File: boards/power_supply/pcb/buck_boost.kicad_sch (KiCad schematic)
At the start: 30 parts

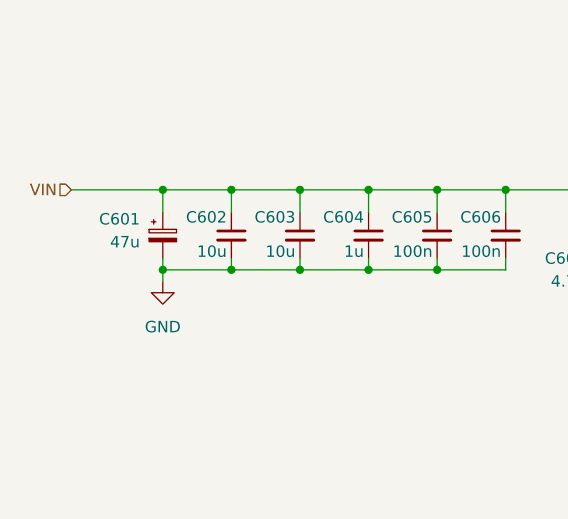
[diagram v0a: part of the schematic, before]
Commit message: psu schematic capture
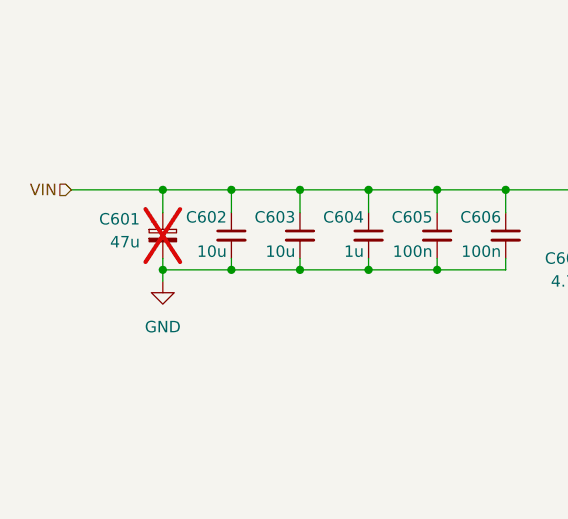
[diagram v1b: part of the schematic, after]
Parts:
- C601: now not fitted
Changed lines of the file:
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@@
 		(in_bom yes)
 		(on_board yes)
-		(dnp no)
+		(dnp yes)
 		(property "Reference" "C601"
 			(at 52.07 79.4638 0)

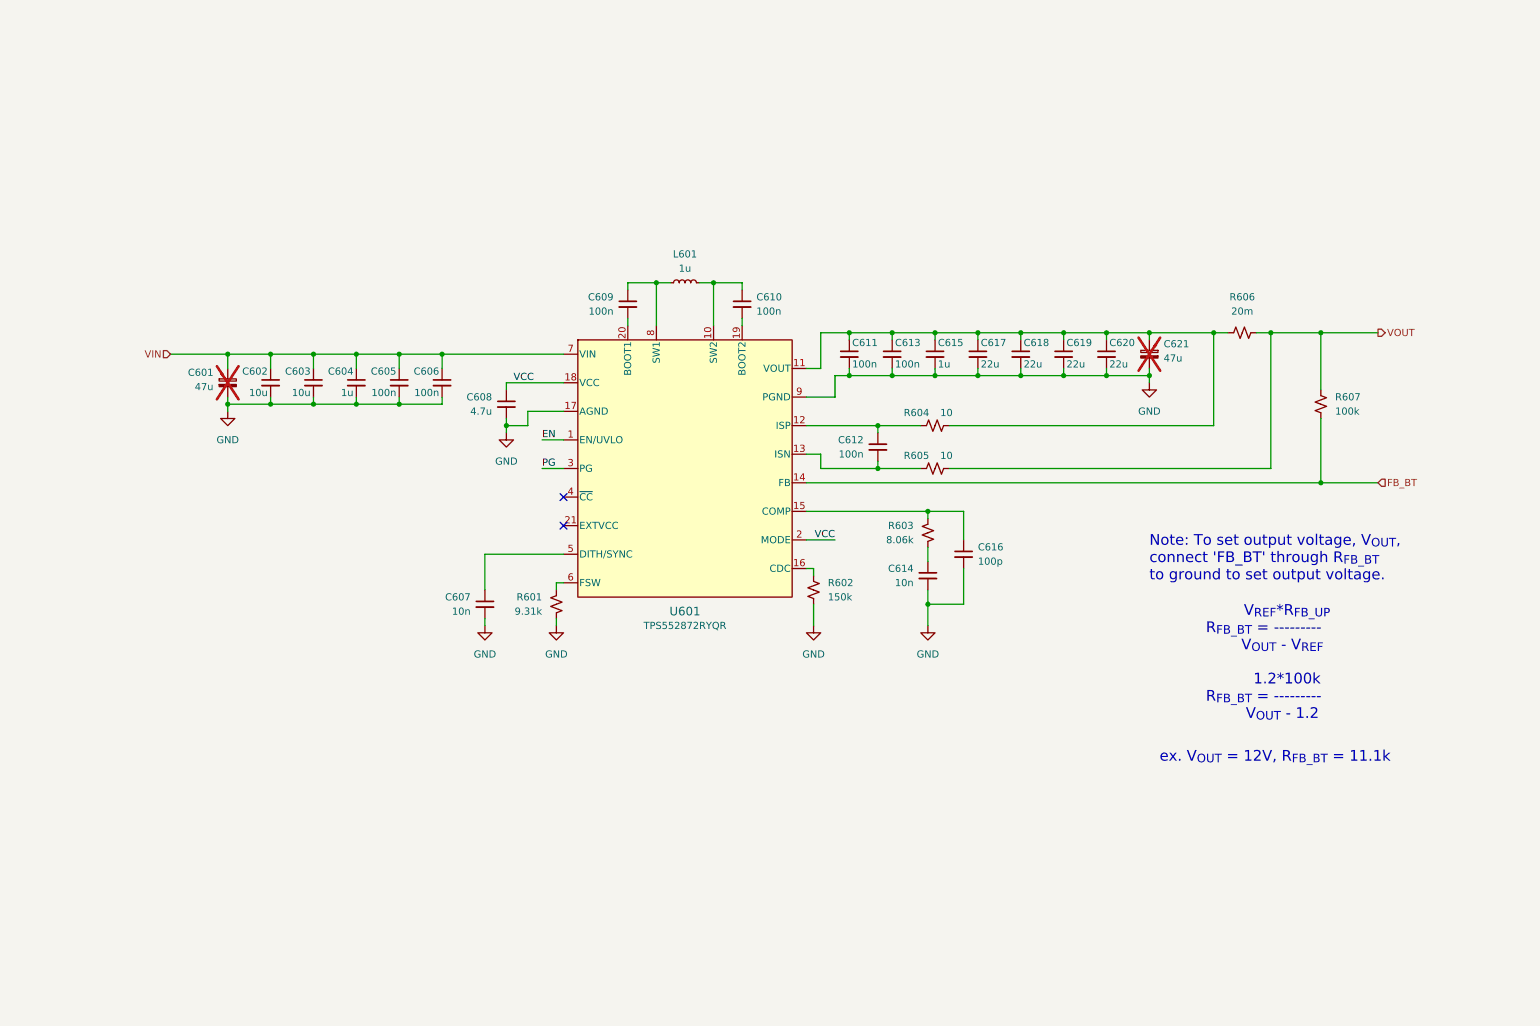
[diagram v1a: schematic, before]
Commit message: psu schematic capture
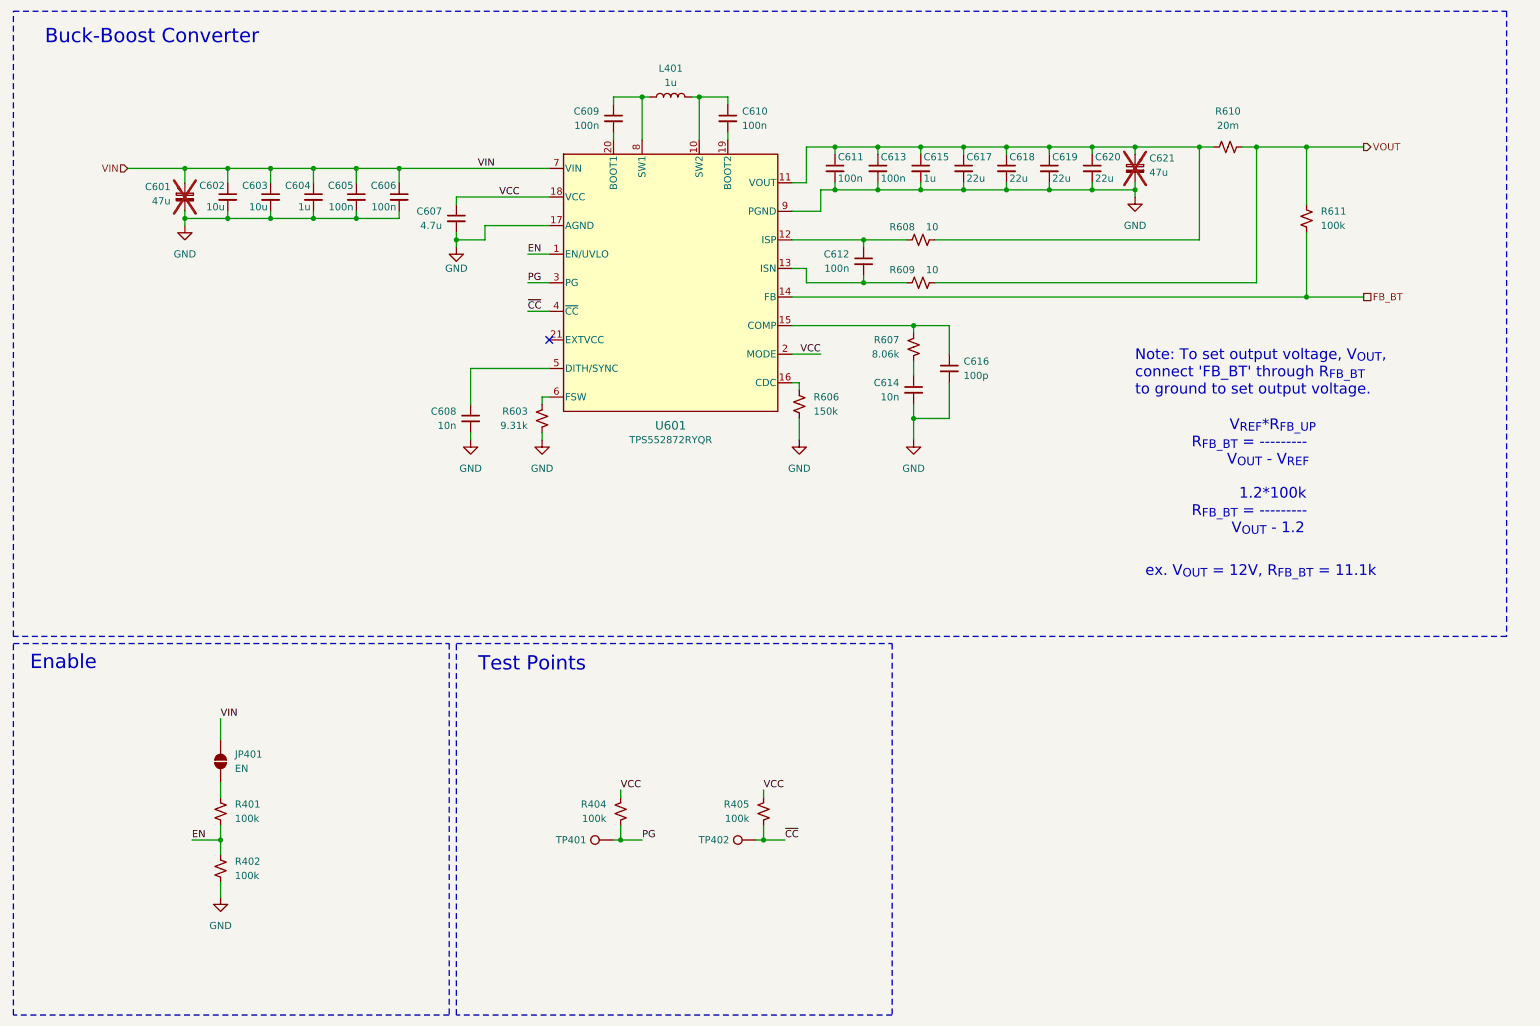
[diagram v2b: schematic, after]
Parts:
- removed L601: 1u, symbol Device:L_Small
- added JP401: EN, symbol Jumper:SolderJumper_2_Open
- added L401: 1u, symbol Device:L
- added R401, R402, R404, R405: 100k, symbol Device:R_Small_US
- added TP401, TP402: TestPoint, symbol Connector:TestPoint
- renumbered C608 to C607, C607 to C608, R601 to R603, R602 to R606, R603 to R607, R604 to R608, R605 to R609, R606 to R610, R607 to R611
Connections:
- net EN: now also R401.2, R402.1
- net GND: now also R402.2
- net PG: now also R404.2, TP401.1
- net VCC: now also R404.1, R405.1
- net VIN: now also JP401.2 (B)
- net at C610.1, U601.10 (SW2): now also L401.2
- net at C609.1, U601.8 (SW1): now also L401.1
- net ~{CC}: now reaches U601.4 (~{CC})
- net ~{CC}: now also R405.2, TP402.1
- new net: JP401.1 (A), R401.1
- no-connect marks 2 -> 1
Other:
- note added: "Buck-Boost Converter"
- note added: "Enable"
- note added: "Test Points"
- moved on the sheet: C601, C602, C603, C604, C605, C606, C607, C608, C609, C610, C611, C612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

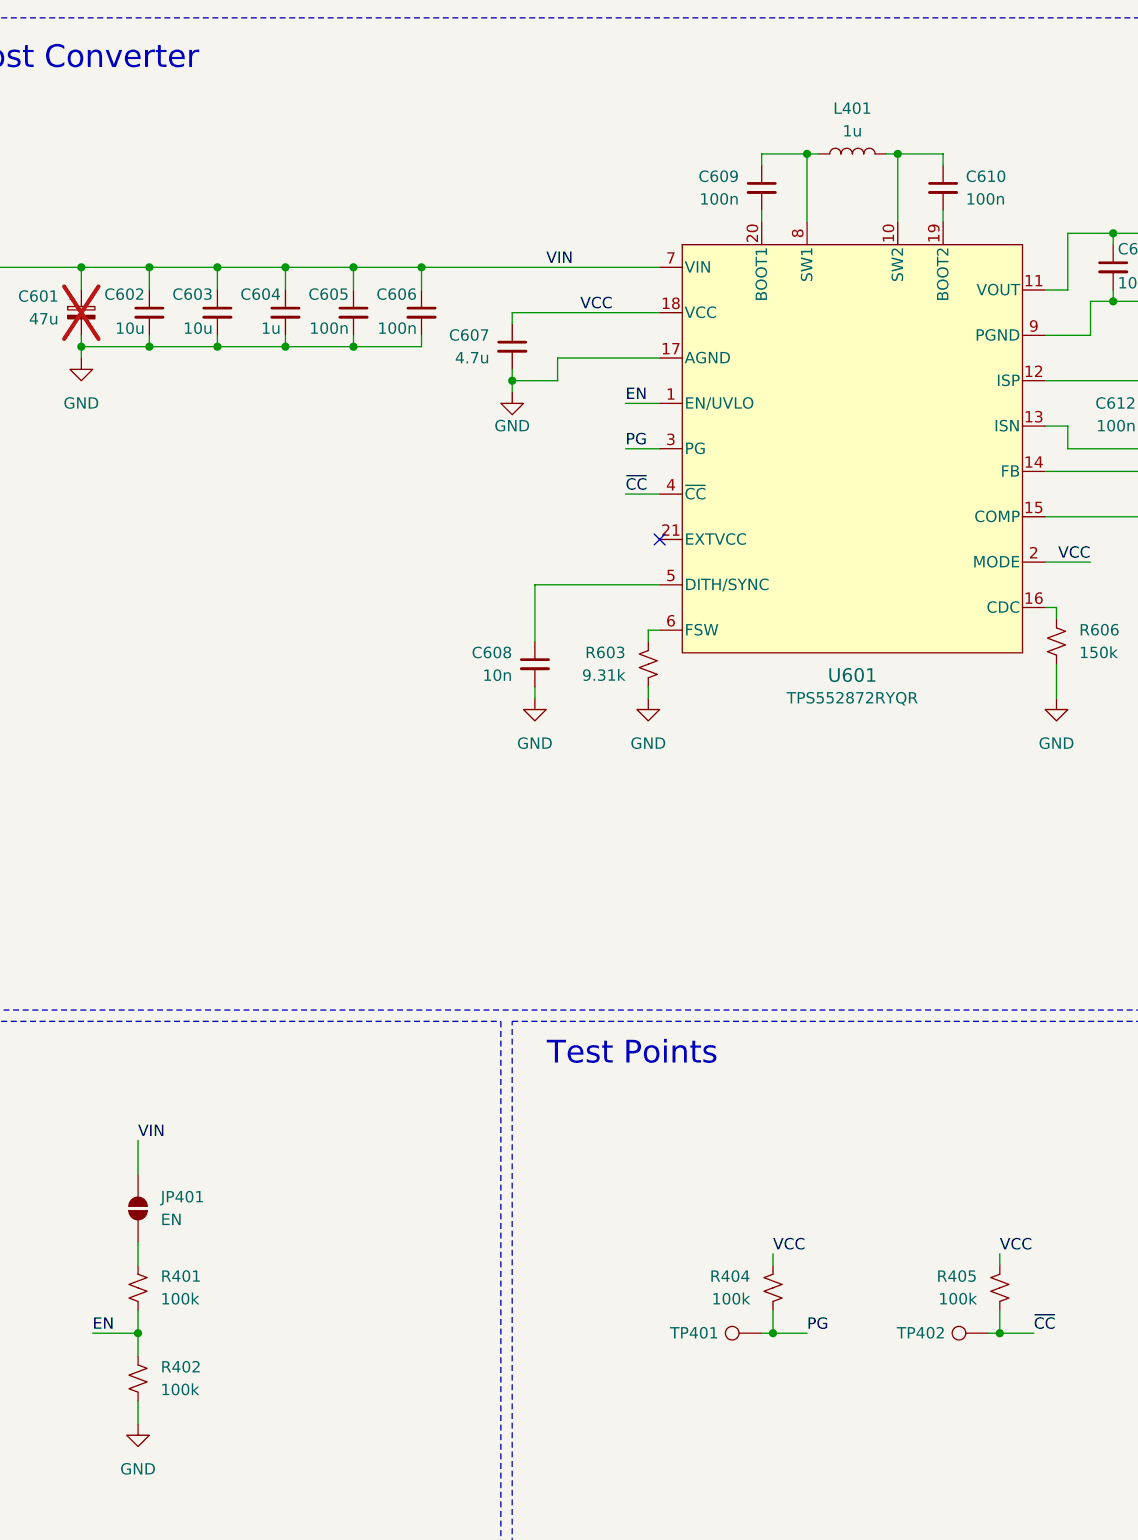
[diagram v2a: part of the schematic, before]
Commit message: psu component selection
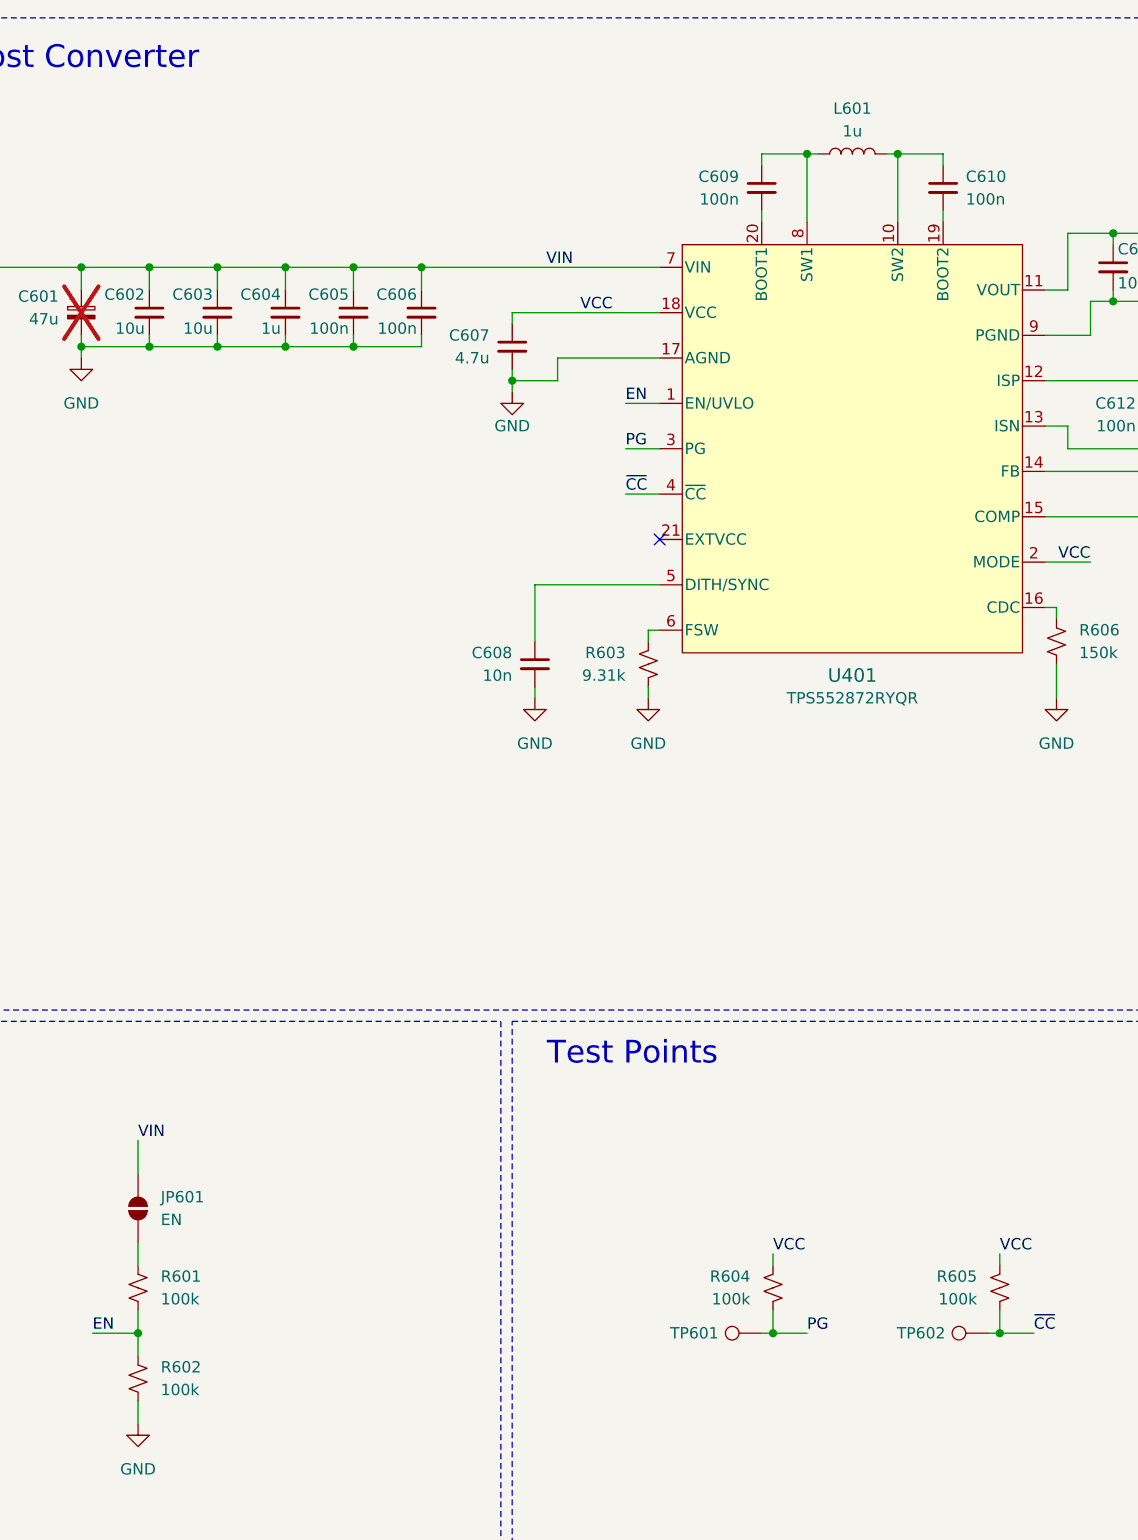
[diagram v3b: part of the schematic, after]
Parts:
- removed U601: ~, VQFN21_RYQ_TEX, symbol TPS552872RYQR:TPS552872RYQR
- added U401: ~, VQFN21_RYQ_TEX, symbol TPS552872RYQR:TPS552872RYQR
- renumbered JP401 to JP601, L401 to L601, R401 to R601, R402 to R602, R404 to R604, R405 to R605, TP401 to TP601, TP402 to TP602
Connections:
- net EN: now also U401.1 (EN/UVLO)
- net FB_BT: now also U401.14 (FB)
- net GND: now also U401.17 (AGND), U401.9 (PGND)
- net PG: now also U401.3 (PG)
- net VCC: now also U401.18 (VCC), U401.2 (MODE)
- net VIN: now also U401.7 (VIN)
- net ~{CC}: now also U401.4 (~{CC})
- net at R606.1: now also U401.16 (CDC)
- net at C611.1, C613.1, C615.1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: now also U401.11 (VOUT)
- net at C612.2, R609.2: now also U401.13 (ISN)
- net at C616.1, R607.1: now also U401.15 (COMP)
- net at C610.1, L601.2: now also U401.10 (SW2)
- net at C610.2: now also U401.19 (BOOT2)
- net at C608.1: now also U401.5 (DITH/SYNC)
- net at C609.1, L601.1: now also U401.8 (SW1)
- net at C609.2: now also U401.20 (BOOT1)
- net at C612.1, R608.2: now also U401.12 (ISP)
- net at R603.1: now also U401.6 (FSW)
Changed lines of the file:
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@@
 		(dnp no)
 		(fields_autoplaced yes)
-		(property "Reference" "#PWR0402"
+		(property "Reference" "#PWR0602"
 			(at 53.34 179.07 0)
 			(effects
@@
 	)
 	(symbol
+		(lib_id "TPS552872RYQR:TPS552872RYQR")
+		(at 111.76 43.18 0)
+		(unit 1)
+		(exclude_from_sim no)
+		(in_bom yes)
+		(on_board yes)
+		(dnp no)
+		(fields_autoplaced yes)
+		(property "Reference" "U401"
+			(at 133.35 88.9 0)
+			(effects
+				(font
+					(size 1.524 1.524)
+				)
+			)
+		)
+		(property "Value" "~"
+			(at 132.842 90.424 0)
+			(effects
+				(font
+					(size 1.524 1.524)
+				)
+				(hide yes)
+			)
+		)
+		(property "Footprint" "VQFN21_RYQ_TEX"
+			(at 133.35 93.98 0)
+			(effects
+				(font
+					(size 1.524 1.524)
+				)
+				(hide yes)
+			)
+		)
+		(property "Datasheet" "https://www.ti.com/lit/ds/symlink/tps552872.pdf?ts=1701344503514&ref_url=https%253A%252F%252Fwww.ti.com%252Fproduct%252FTPS552872"
+			(at 131.826 27.432 0)
+			(effects
+				(font
+					(size 1.524 1.524)
+				)
+				(hide yes)
+			)
+		)
+		(property "Description" "Buck-Boost Switching Regulator IC Positive Adjustable 0.8V 1 Output 2.5A 21-PowerVFQFN"
+			(at 130.81 24.384 0)
+			(effects
+				(font
+					(size 1.27 1.27)
+				)
+				(hide yes)
+			)
+		)
+		(property "MPN" "TPS552872RYQR"
+			(at 133.35 91.44 0)
+			(effects
+				(font
+					(size 1.27 1.27)
+				)
+			)
+		)
+		(pin "20"
+		)
+		(pin "21"
+		)
+		(pin "15"
+		)
+		(pin "7"
+		)
+		(pin "12"
+		)
+		(pin "3"
+		)
+		(pin "18"
+		)
+		(pin "2"
+		)
+		(pin "16"
+		)
+		(pin "1"
+		)
+		(pin "5"
+		)
+		(pin "19"
+		)
+		(pin "14"
+		)
+		(pin "9"
+		)
+		(pin "4"
+		)
+		(pin "8"
+		)
+		(pin "6"
+		)
+		(pin "11"
+		)
+		(pin "17"
+		)
+		(pin "13"
+		)
+		(pin "10"
+		)
+		(instances
+			(project ""
+				(path "/6a7d9dc9-f78f-470f-911b-b95256023173/c2fcbfb1-6741-44cb-a82c-7741918cd8a1"
+					(reference "U601")
+					(unit 1)
+				)
+				(path "/6a7d9dc9-f78f-470f-911b-b95256023173/cf53f1a5-f32c-4d02-84d0-a76cca0772c3"
+					(reference "U401")
+					(unit 1)
+				)
+				(path "/6a7d9dc9-f78f-470f-911b-b95256023173/d1fcefd7-3ecc-4716-9879-f129c42734ff"
+					(reference "U501")
+					(unit 1)
+				)
+			)
+		)
+	)
+	(symbol
 		(lib_id "Device:C_Small")
 		(at 95.25 52.07 0)
@@
 		(dnp no)
 		(fields_autoplaced yes)
-		(property "Reference" "R402"
+		(property "Reference" "R602"
 			(at 55.88 166.3699 0)
 			(effects
@@
 		(dnp no)
 		(fields_autoplaced yes)
-		(property "Reference" "R401"
+		(property "Reference" "R601"
 			(at 55.88 156.2099 0)
 			(effects
@@
 		(on_board yes)
 		(dnp no)
-		(property "Reference" "TP402"
+		(property "Reference" "TP602"
 			(at 143.764 162.56 90)
 			(effects
@@
 		(on_board yes)
 		(dnp no)
-		(property "Reference" "JP401"
+		(property "Reference" "JP601"
 			(at 55.88 147.3199 90)
 			(effects
@@
 		(on_board yes)
 		(dnp no)
-		(property "Reference" "TP401"
+		(property "Reference" "TP601"
 			(at 118.364 162.56 90)
 			(effects
@@
 		(on_board yes)
 		(dnp no)
-		(property "Reference" "R404"
+		(property "Reference" "R604"
 			(at 121.92 156.2099 0)
 			(effects
@@
 		(dnp no)
 		(fields_autoplaced yes)
-		(property "Reference" "L401"
+		(property "Reference" "L601"
 			(at 133.35 25.4 90)
 			(effects
@@
 	)
 	(symbol
-		(lib_id "TPS552872RYQR:TPS552872RYQR")
-		(at 111.76 43.18 0)
-		(unit 1)
-		(exclude_from_sim no)
-		(in_bom yes)
-		(on_board yes)
-		(dnp no)
-		(fields_autoplaced yes)
-		(property "Reference" "U601"
-			(at 133.35 88.9 0)
-			(effects
-				(font
-					(size 1.524 1.524)
-				)
-			)
-		)
-		(property "Value" "~"
-			(at 132.842 90.424 0)
-			(effects
-				(font
-					(size 1.524 1.524)
-				)
-				(hide yes)
-			)
-		)
-		(property "Footprint" "VQFN21_RYQ_TEX"
-			(at 133.35 95.25 0)
-			(effects
-				(font
-					(size 1.524 1.524)
-				)
-				(hide yes)
-			)
-		)
-		(property "Datasheet" "https://www.ti.com/lit/ds/symlink/tps552872.pdf?ts=1701344503514&ref_url=https%253A%252F%252Fwww.ti.com%252Fproduct%252FTPS552872"
-			(at 131.826 27.432 0)
-			(effects
-				(font
-					(size 1.524 1.524)
-				)
-				(hide yes)
-			)
-		)
-		(property "Description" "Buck-Boost Switching Regulator IC Positive Adjustable 0.8V 1 Output 2.5A 21-PowerVFQFN"
-			(at 130.81 24.384 0)
-			(effects
-				(font
-					(size 1.27 1.27)
-				)
-				(hide yes)
-			)
-		)
-		(property "MPN" "TPS552872RYQR"
-			(at 133.35 91.44 0)
-			(effects
-				(font
-					(size 1.27 1.27)
-				)
-			)
-		)
-		(pin "5"
-		)
-		(pin "16"
-		)
-		(pin "7"
-		)
-		(pin "12"
-		)
-		(pin "11"
-		)
-		(pin "2"
-		)
-		(pin "15"
-		)
-		(pin "6"
-		)
-		(pin "4"
-		)
-		(pin "21"
-		)
-		(pin "8"
-		)
-		(pin "20"
-		)
-		(pin "18"
-		)
-		(pin "10"
-		)
-		(pin "3"
-		)
-		(pin "9"
-		)
-		(pin "19"
-		)
-		(pin "13"
-		)
-		(pin "17"
-		)
-		(pin "1"
-		)
-		(pin "14"
-		)
-		(instances
-			(project "power_supply"
-				(path "/6a7d9dc9-f78f-470f-911b-b95256023173/c2fcbfb1-6741-44cb-a82c-7741918cd8a1"
-					(reference "U601")
-					(unit 1)
-				)
-				(path "/6a7d9dc9-f78f-470f-911b-b95256023173/cf53f1a5-f32c-4d02-84d0-a76cca0772c3"
-					(reference "U401")
-					(unit 1)
-				)
-				(path "/6a7d9dc9-f78f-470f-911b-b95256023173/d1fcefd7-3ecc-4716-9879-f129c42734ff"
-					(reference "U501")
-					(unit 1)
-				)
-			)
-		)
-	)
-	(symbol
 		(lib_id "Device:R_Small_US")
 		(at 176.53 74.93 0)
@@
 		(on_board yes)
 		(dnp no)
-		(property "Reference" "R405"
+		(property "Reference" "R605"
 			(at 147.32 156.2099 0)
 			(effects
